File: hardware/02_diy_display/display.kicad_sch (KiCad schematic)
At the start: 13 parts, among them J1 Connector_1, U1 mini DS3231 module, U2 ESP32C3_SUPER_MINI

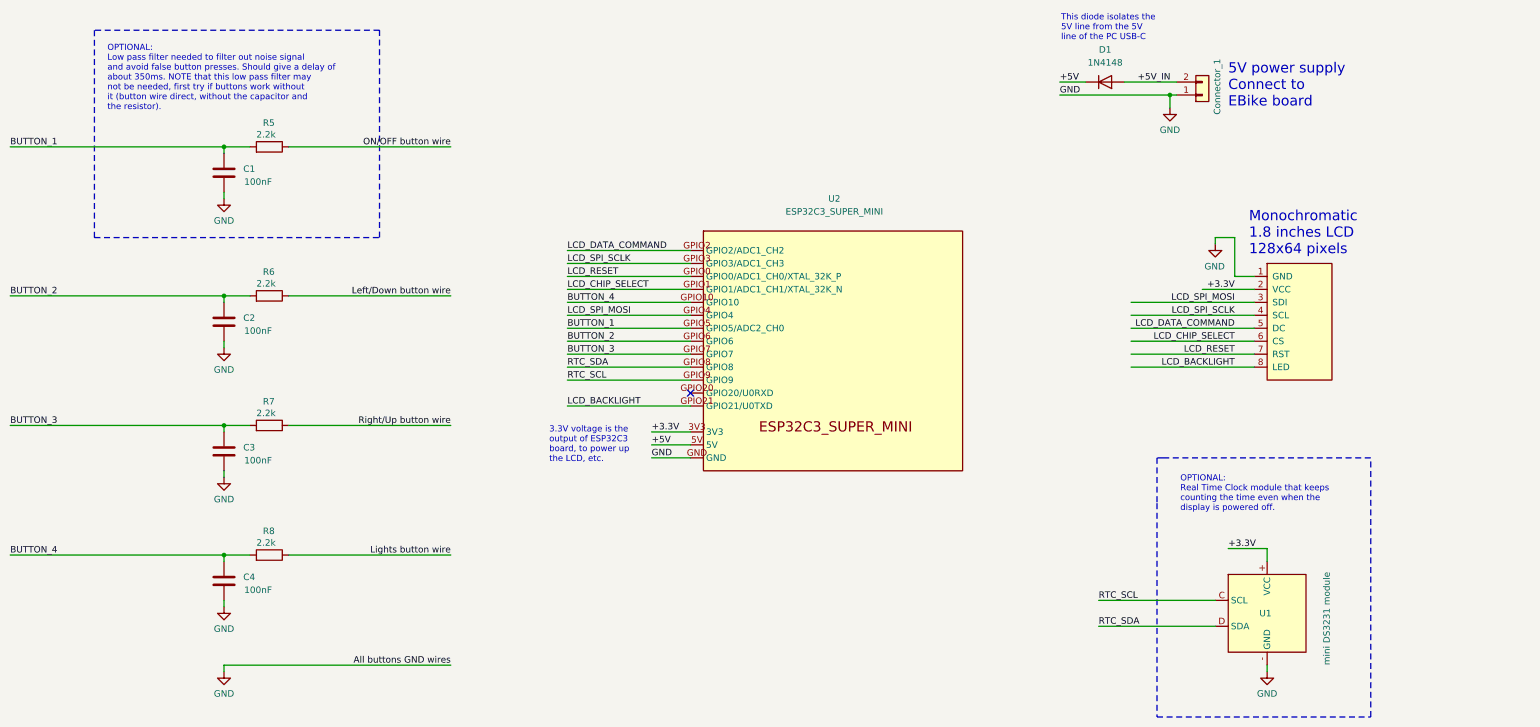
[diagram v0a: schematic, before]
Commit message: Display: changed schematic to use ESP32-S3 instead of ESP32-C3
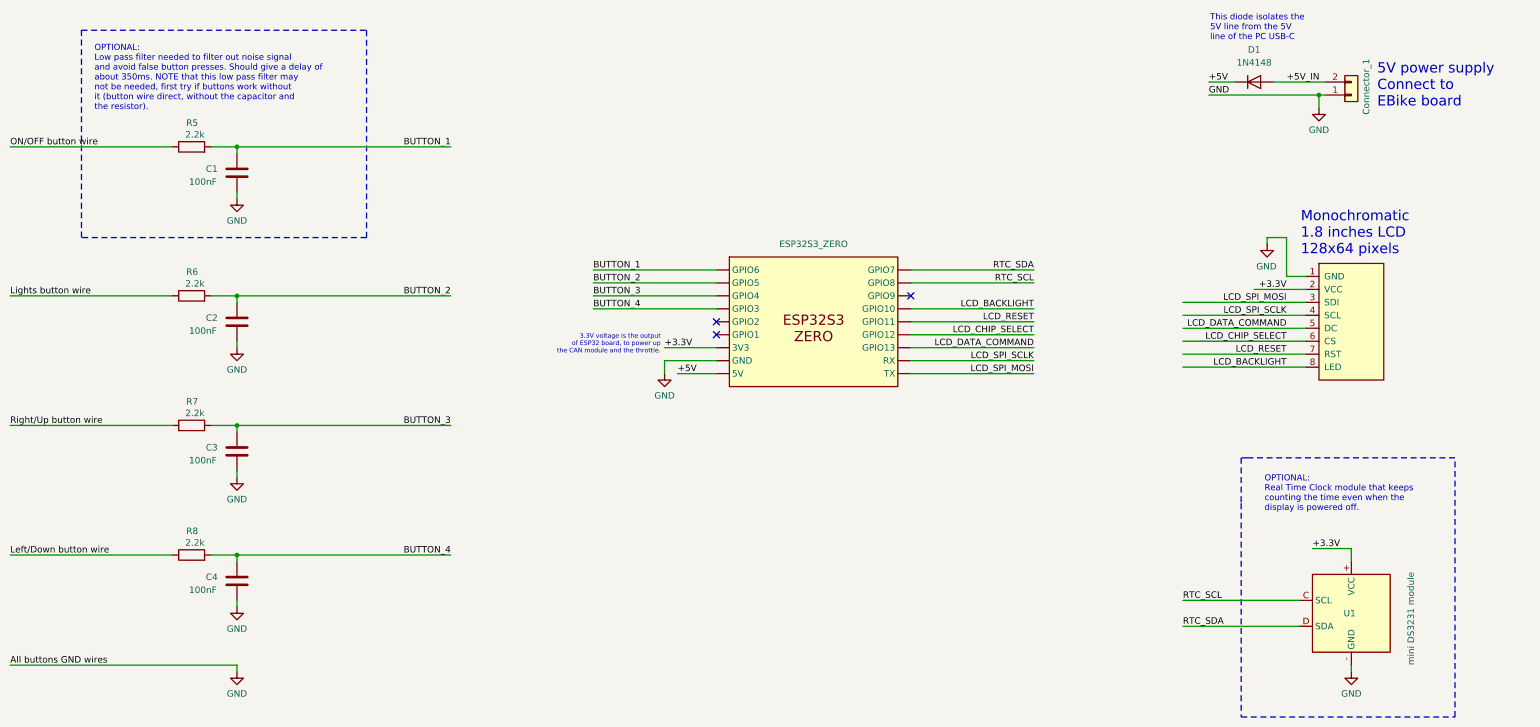
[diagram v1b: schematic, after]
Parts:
- removed U2: ESP32C3_SUPER_MINI, symbol Espressif:ESP32-C3-MINI-1
- added U3: ESP32S3_ZERO, symbol esp32-s3-zero:ESP32-C3-MINI-1
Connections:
- net +3.3V: now also U3. (TX)
- net +5V: now also U3. (TX)
- net BUTTON_1: now also U3. (TX)
- net BUTTON_2: now also U3. (TX)
- net BUTTON_3: now also U3. (TX)
- net BUTTON_4: now also U3. (TX)
- net GND: now also U3. (TX)
- net LCD_BACKLIGHT: now also U3. (TX)
- net LCD_CHIP_SELECT: now also U3. (TX)
- net LCD_DATA_COMMAND: now also U3. (TX)
- net LCD_RESET: now also U3. (TX)
- net LCD_SPI_MOSI: now also U3. (TX)
- net LCD_SPI_SCLK: now also U3. (TX)
- net Left/Down button wire: now also R8.1; no longer R6.1
- net Lights button wire: now also R6.1; no longer R8.1
- net RTC_SCL: now also U3. (TX)
- net RTC_SDA: now also U3. (TX)
- no-connect marks 1 -> 3
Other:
- note added: "3.3V voltage is the output of ESP32 board, to power up the CAN module and the throttle."
- note removed: "3.3V voltage is the output of ESP32C3 board, to power up the LCD, etc."
- moved on the sheet: C1, C2, C3, C4, D1, R5, R6, R7, R8, U1
